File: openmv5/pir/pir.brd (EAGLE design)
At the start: 35.6 x 44.4 mm, 51 parts, among them IC1 AG9905LP, J1 GMJXHT-MM-S-88, J2 OPENMV5-BOTTOM, T1 PT61018PEL

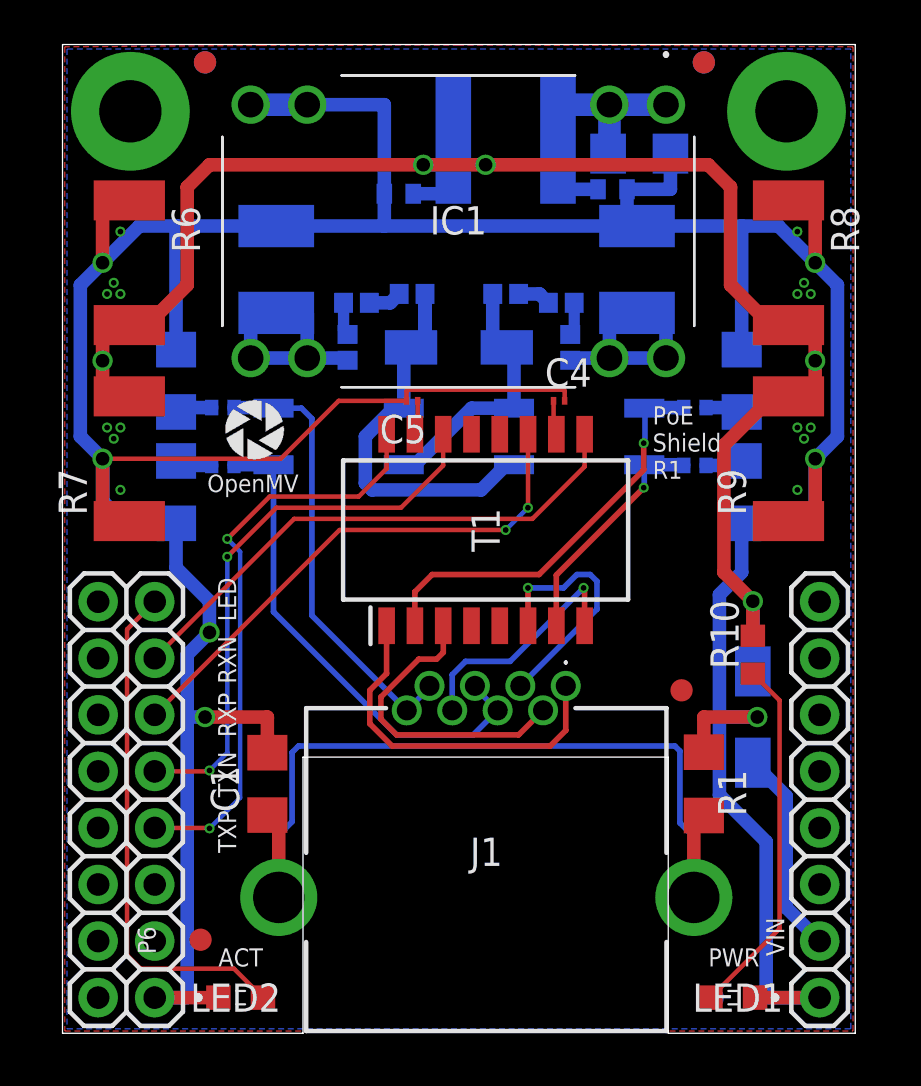
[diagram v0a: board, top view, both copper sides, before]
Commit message: Update PoE Shield heat transfer and add PIR Shield
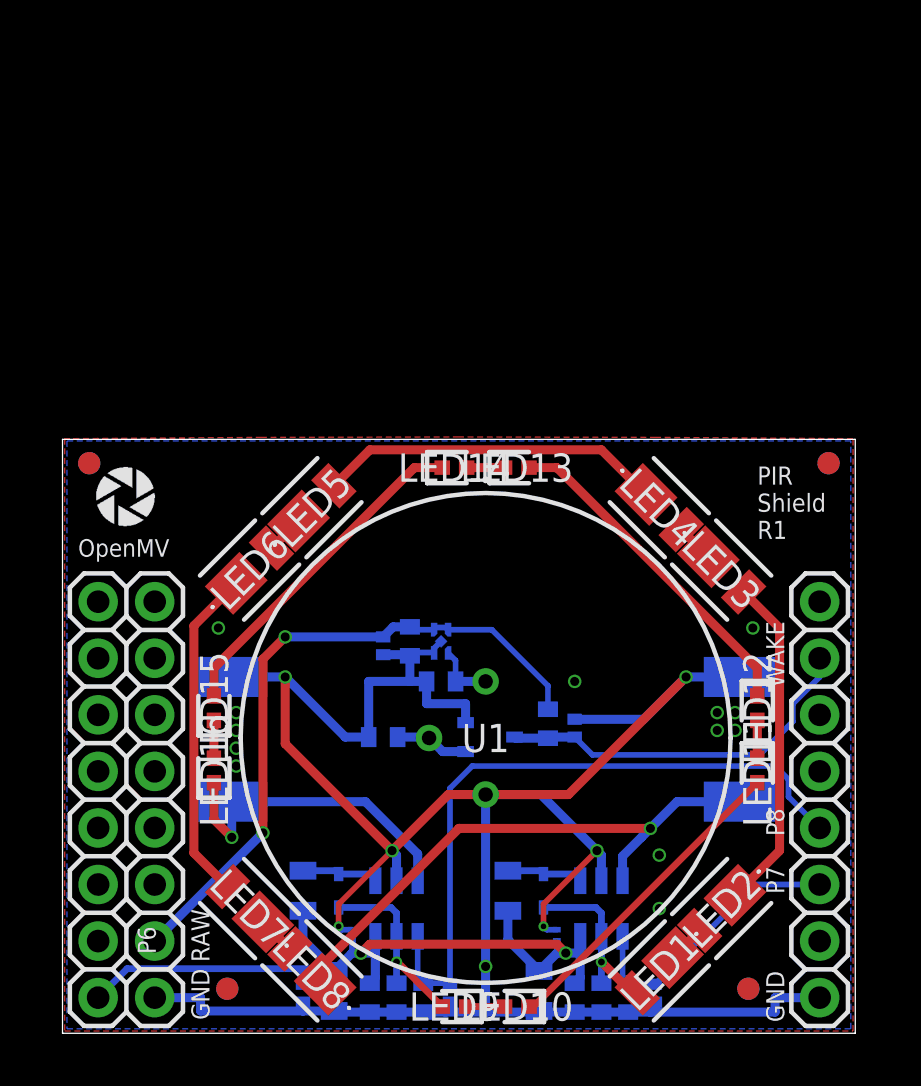
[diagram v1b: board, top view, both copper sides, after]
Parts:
- removed BR1, BR2: MB6S-TP, MB6S-TP:SOP254P665X270-4N
- removed C10, C12, C8, C9: 1nF, rcl:C1206
- removed C11: 10uF, rcl:C0402
- removed J1: GMJXHT-MM-S-88, GMJXHT-MM-S-88:GMJXHTMMS88
- removed L3, L4, L5, L6: 1k, SparkFun-Coils:0402
- removed L7: NR6045T1R8N, NR6045T1R8N:NR6045T1R8N
- removed R10: 470, rcl:R0603
- removed R5: 75, rcl:R0402
- removed R6, R7, R8, R9: 100, rcl:R2512
- removed T1: PT61018PEL, PT61018PEL:SOIC127P930X565-16N
- added C46: 4.7uF, sfe:0402-CAP
- added C48: 0.22uF, rcl:C0201
- added C49: 22uF, SparkFun-Capacitors:0805
- added D3, D4, D6, D9: CPDQT5V0HE-HF, CPDQT5V0HE-HF:CPDQT5V0HEHF
- added D5: RB520S30T5G, RB520S30T5G:SODFL1608X70N
- added IC2: AP3032KTR-G1, AP3032KTR-G1:SOT95P280X145-6N
- added LED10, LED11, LED12, LED13, LED14, LED15, LED16, LED9: SFH_4053, SFH_4053:LEDC1005X55N
- added LED3, LED4, LED5, LED6, LED7, LED8: JB2835AWT-W-U57EA0000-N0000001, JB2835AWT-W-U57EA0000-N0000001:JB2835AWTWU57EA0000N0000001
- added Q4: 2N7002KW_R1_00001, 2N7002KW_R1_00001:SOT65P210X110-3N
- added R24: 100K, sfe:0402-RES
- added R26: 1K, sfe:0402-RES
- added U1: EKMB1307113K, EKMB1304111K:EKMB1304111K
- added U2: MIC5365-3.3YMT-TZ, MIC5365-3.3YMT-TZ:VREG_MIC5365-3.3YMT-TZ
- C1: value 1nF -> 4.7uF; device rcl:C1206 -> sfe:0402-CAP
- C2: value 4.7nF -> 4.7uF; device rcl:C1812 -> sfe:0402-CAP
- C3: value 4.7nF -> 1uF; device rcl:C1812 -> sfe:0402-CAP
- C4: value 0.1uF -> 22uF; device rcl:C0201 -> SparkFun-Capacitors:0805
- C5: value 0.1uF -> 0.22uF
- C6: value 100uF -> 4.7uF; device rcl:C1206 -> sfe:0402-CAP
- C7: value 10uF -> 1uF; device rcl:C0402 -> sfe:0402-CAP
- D1: value SMAJ58A-13-F -> CPDQT5V0HE-HF; device SMAJ58A-13-F:DIOM5226X230N -> CPDQT5V0HE-HF:CPDQT5V0HEHF
- D2: value FM240A -> RB520S30T5G; device FM240A:DIOM5025X231N -> RB520S30T5G:SODFL1608X70N
- IC1: value AG9905LP -> AP3032KTR-G1; device Ag9905LP:AG9905LP -> AP3032KTR-G1:SOT95P280X145-6N
- J2: value OPENMV5-BOTTOM -> OPENMV5-TOP; device openmv5:OPENMV5-BOTTOM -> openmv5:OPENMV5-TOP
- L1, L2: value 1k -> 6.8uH; device SparkFun-Coils:0402 -> SparkFun-Coils:0805
- LED1: value LTST-S270KSKT -> JB2835AWT-W-U57EA0000-N0000001; device LTST-S270K:LTSTS270K -> JB2835AWT-W-U57EA0000-N0000001:JB2835AWTWU57EA0000N0000001
- LED2: value LTST-S270KGKT -> JB2835AWT-W-U57EA0000-N0000001; device LTST-S270K:LTSTS270K -> JB2835AWT-W-U57EA0000-N0000001:JB2835AWTWU57EA0000N0000001
- R1: value 1M -> 100K; device rcl:R1206 -> sfe:0402-RES
- R2, R4: value 75 -> 3.9; device rcl:R0402 -> rcl:R2512
- R3: value 75 -> 100K; device rcl:R0402 -> sfe:0402-RES
- moved C6 39.8 mm to (13.8, 1.60), turned to 90 degrees
- moved C7 37.6 mm to (15.0, 1.60), turned to 90 degrees
- moved IC1 36.2 mm to (24.2, 5.60), flipped to the bottom, turned to 270 degrees
- moved C3 35.8 mm to (24.2, 1.60)
- moved C4 28.4 mm to (12.2, 1.90), flipped to the bottom, turned to 90 degrees
- moved L2 27.2 mm to (10.8, 6.40), turned to 90 degrees
- moved R3 26.8 mm to (16.2, 1.60), turned to 270 degrees
- moved L1 26.8 mm to (20.0, 6.40), turned to 90 degrees
- moved C5 24.2 mm to (13.0, 4.40), flipped to the bottom, turned to 90 degrees
- moved LED2 22.0 mm to (29.6, 5.60), turned to 45 degrees
- moved C2 20.5 mm to (17.0, 15.8), turned to 180 degrees
- moved FD5 18.9 mm to (34.4, 25.6)
- moved FD6 18.9 mm to (34.4, 25.6)
- moved FD7 18.7 mm to (1.20, 25.6)
- moved FD8 18.7 mm to (1.20, 25.6)
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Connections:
- removed net MDI_LED: J2.17, LED2.2
- removed net MDI_RX_CT: C4.1, T1.10
- removed net MDI_RX_N: J2.18, T1.9
- removed net MDI_RX_P: J2.19, T1.11
- removed net MDI_TX_CT: C5.1, T1.15
- removed net MDI_TX_N: J2.20, T1.14
- removed net MDI_TX_P: J2.21, T1.16
- removed net NC1: T1.4
- removed net NC2: T1.5
- removed net NC3: T1.12
- removed net NC4: T1.13
- removed net POE_VIN_INT_N: C2.1, IC1.7, IC1.8, L5.2
- removed net POE_VIN_INT_P: C3.1, IC1.5, IC1.6, L6.2
- removed net POE_VIN_N: BR1.4, BR2.4, D1.2, L1.1
- removed net POE_VIN_N0: L1.2, L3.1
- removed net POE_VIN_N1: L3.2, L5.1
- removed net POE_VIN_P: BR1.3, BR2.3, D1.1, L2.1
- removed net POE_VIN_P0: L2.2, L4.1
- removed net POE_VIN_P1: L4.2, L6.1
- removed net RX_N: J1.6, T1.8
- removed net RX_P: J1.3, T1.6
- removed net SHIELD_GND: C1.1, J1.MH1, J1.MH2, R1.2
- removed net TX_N: J1.2, T1.3
- removed net TX_P: J1.1, T1.1
- removed net VA1: BR1.1, R2.2, T1.2
- removed net VA1_ISO: C8.1, R2.1
- removed net VA2: BR1.2, R3.2, T1.7
- removed net VA2_ISO: C9.1, R3.1
- removed net VB1: BR2.1, J1.4, J1.5, R4.2
- removed net VB1_ISO: C10.1, R4.1
- removed net VB2: BR2.2, J1.7, J1.8, R5.2
- removed net VB2_ISO: C12.1, R5.1
- removed net VDC: C6.1, C7.1, IC1.1, IC1.2, L7.1
- removed net VIN: C11.1, D2.2, L7.2, R10.2, R6.2, R7.2, R8.2, R9.2
- removed net VIN_INT: D2.1, J2.10
- removed net VIN_LED: LED1.2, R10.1
- new net I1: LED10.2, LED9.1
- new net I2: LED10.1, LED11.2
- new net I3: LED11.1, LED12.2
- new net I4: LED12.1, LED13.2
- new net I5: LED13.1, LED14.2
- new net I6: LED14.1, LED15.2
- new net I7: LED15.1, LED16.2
- new net IFB: IC2.3, LED16.1, R4.2
- new net IOV: C7.2, D5.1, IC2.5, LED9.2
- new net ISW: D5.2, IC2.1, L2.2
- new net OUT: Q4.1, R24.1, U1.2
- new net P11_WAKEUP: D9.1, J2.15, Q4.3, R26.1
- new net P7_PWM: D3.1, IC1.4, J2.11, R1.1
- new net P8_PWM: D6.1, IC2.4, J2.12, R3.1
- new net RAW: C1.2, D1.1, J2.23, R26.2, U2.3, U2.4
- new net VCC: C4.2, C46.2, C48.1, C49.2, C5.1, C6.2, D4.1, IC1.6, IC2.6, J2.8, L1.1, L2.1
- new net VDD: C2.2, U1.1, U2.1
- new net W1: LED1.1, LED2.2
- new net W2: LED2.1, LED3.2
- new net W3: LED3.1, LED4.2
- new net W4: LED4.1, LED5.2
- new net W5: LED5.1, LED6.2
- new net W6: LED6.1, LED7.2
- new net W7: LED7.1, LED8.2
- new net WFB: IC1.3, LED8.1, R2.2
- new net WOV: C3.2, D2.1, IC1.5, LED1.2
- new net WSW: D2.2, IC1.1, L1.2
- net GND: now also C1.1, C2.1, C3.1, C4.1, C46.1, C48.2, C49.1, C6.1, C7.1, D1.2, D3.2, D4.2, D6.2, D9.2, IC1.2, IC2.2, Q4.2, R1.2, R2.1, R24.2, R3.2, R4.1, U1.3, U2.2, U2.EP; no longer C1.2, C10.2, C11.2, C12.2, C2.2, C3.2, C4.2, C6.2, C7.2, C8.2, C9.2, IC1.3, IC1.4, LED1.1, LED2.1, R1.1, R6.1, R7.1, R8.1, R9.1
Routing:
- net GND: track 196.3 -> 116.2 mm, vias 23 -> 20
- net VIN: track 74.6 -> 0.00 mm, vias 5 -> 0
- net VCC: track 0.00 -> 39.2 mm, vias 0 -> 2
- net SHIELD_GND: track 39.0 -> 0.00 mm
- net P8_PWM: track 0.00 -> 30.8 mm
- net RAW: track 0.00 -> 30.4 mm, vias 0 -> 2
- net MDI_TX_P: track 26.3 -> 0.00 mm, vias 2 -> 0
- net WFB: track 0.00 -> 25.4 mm, vias 0 -> 1
- net MDI_TX_N: track 25.2 -> 0.00 mm, vias 2 -> 0
- net MDI_RX_N: track 24.3 -> 0.00 mm
- net MDI_RX_P: track 23.9 -> 0.00 mm, vias 2 -> 0
- net MDI_LED: track 23.3 -> 0.00 mm
- net VB1: track 22.7 -> 0.00 mm
- net POE_VIN_P: track 20.3 -> 0.00 mm
- net VB2: track 20.1 -> 0.00 mm
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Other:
- board size 35.6 x 44.4 mm -> 35.6 x 26.7 mm
- board text added: "3.31.23"
- board text added: "P7"
- board text added: "P8"
- board text added: "PIR Shield R1"
- board text added: "RAW"
- board text added: "WAKE"
- board text removed: "3.26.23"
- board text removed: "ACT"
- board text removed: "LED"
- board text removed: "PWR"
- board text removed: "PoE Shield R1"
- board text removed: "RXN"
- board text removed: "RXP"
- board text removed: "TXN"
- board text removed: "TXP"
- board text removed: "VIN"

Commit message: Renumber parts
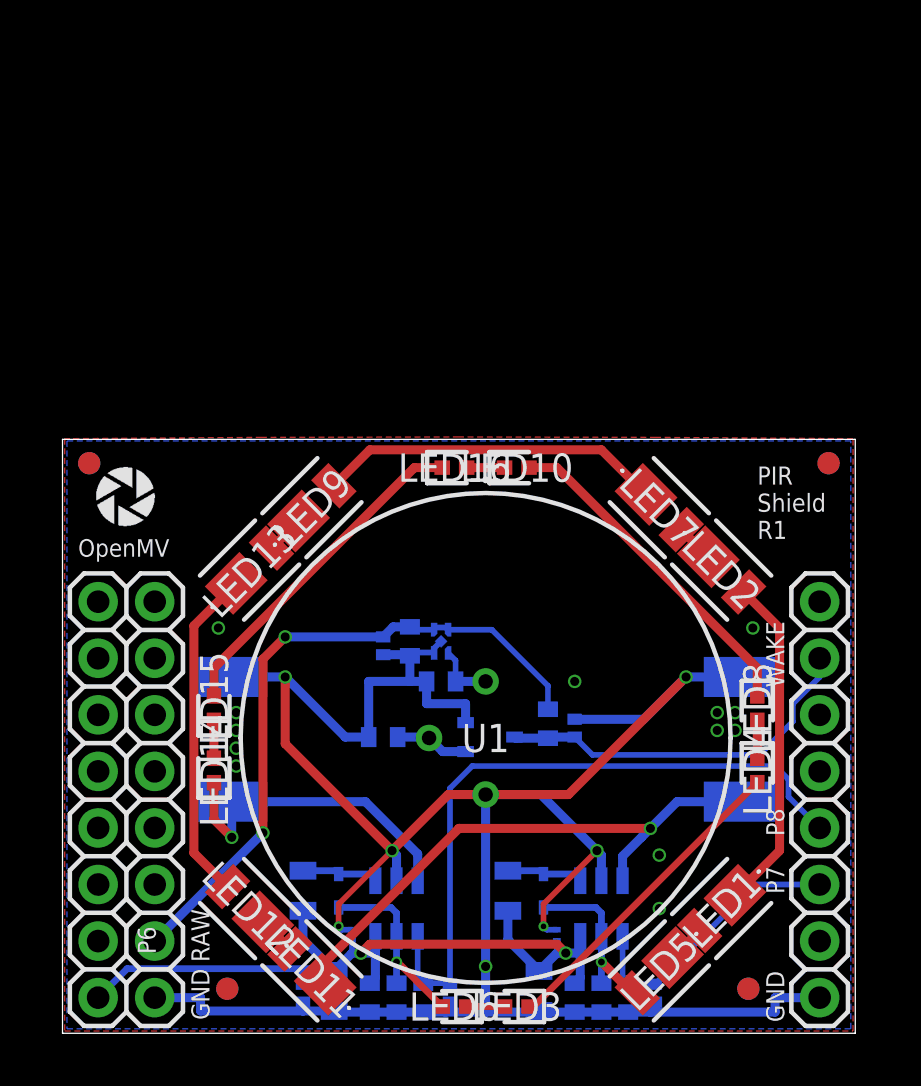
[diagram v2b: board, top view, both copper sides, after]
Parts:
- removed C46: 4.7uF, sfe:0402-CAP
- removed C48: 0.22uF, rcl:C0201
- removed C49: 22uF, SparkFun-Capacitors:0805
- removed D9: CPDQT5V0HE-HF, CPDQT5V0HE-HF:CPDQT5V0HEHF
- added C10, C9: 4.7uF, sfe:0402-CAP
- added C8: 1uF, sfe:0402-CAP
- added D7: CPDQT5V0HE-HF, CPDQT5V0HE-HF:CPDQT5V0HEHF
- C1: value 4.7uF -> 22uF; device sfe:0402-CAP -> SparkFun-Capacitors:0805
- C3, C7: value 1uF -> 0.22uF; device sfe:0402-CAP -> rcl:C0201
- C4: value 22uF -> 1uF; device SparkFun-Capacitors:0805 -> sfe:0402-CAP
- C5: value 0.22uF -> 22uF; device rcl:C0201 -> SparkFun-Capacitors:0805
- D1: value CPDQT5V0HE-HF -> RB520S30T5G; device CPDQT5V0HE-HF:CPDQT5V0HEHF -> RB520S30T5G:SODFL1608X70N
- D5: value RB520S30T5G -> CPDQT5V0HE-HF; device RB520S30T5G:SODFL1608X70N -> CPDQT5V0HE-HF:CPDQT5V0HEHF
- LED11, LED12, LED13, LED9: value SFH_4053 -> JB2835AWT-W-U57EA0000-N0000001; device SFH_4053:LEDC1005X55N -> JB2835AWT-W-U57EA0000-N0000001:JB2835AWTWU57EA0000N0000001
- LED3, LED4, LED6, LED8: value JB2835AWT-W-U57EA0000-N0000001 -> SFH_4053; device JB2835AWT-W-U57EA0000-N0000001:JB2835AWTWU57EA0000N0000001 -> SFH_4053:LEDC1005X55N
- moved FD4 37.9 mm to (1.20, 25.6), flipped to the top
- moved FD5 35.9 mm to (7.40, 2.00), flipped to the bottom
- moved FD7 33.2 mm to (34.4, 25.6), flipped to the bottom
- moved LED5 26.0 mm to (26.8, 2.80), turned to 45 degrees
- moved LED7 25.7 mm to (26.8, 23.6), turned to 135 degrees
- moved LED12 24.5 mm to (8.40, 5.60), turned to 315 degrees
- moved LED10 24.2 mm to (20.4, 25.4), turned to 0 degrees
- moved FD3 23.9 mm to (34.4, 25.6)
- moved FD6 23.9 mm to (30.8, 2.00)
- moved FD2 23.4 mm to (30.8, 2.00), flipped to the top
- moved LED9 23.3 mm to (11.2, 23.6), turned to 225 degrees
- moved LED8 23.2 mm to (31.2, 14.6), turned to 270 degrees
- moved LED11 21.9 mm to (11.2, 2.80), turned to 315 degrees
- moved LED3 21.7 mm to (20.4, 1.20), turned to 180 degrees
- moved LED6 21.7 mm to (17.6, 1.20), turned to 180 degrees
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- renumbered J2 to J1, Q4 to Q1, R24 to R6, R26 to R5
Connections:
- net GND: now also C10.1, C3.2, C5.1, C7.2, C8.1, C9.1, D5.2, D7.2; no longer C3.1, C46.1, C48.2, C49.1, C5.2, C7.1, D1.2, D9.2
- net I1: now also LED3.2, LED6.1; no longer LED10.2, LED9.1
- net I2: now also LED3.1, LED4.2; no longer LED10.1, LED11.2
- net I3: now also LED4.1, LED8.2; no longer LED11.1, LED12.2
- net I4: now also LED10.2, LED8.1; no longer LED12.1, LED13.2
- net I5: now also LED10.1, LED16.2; no longer LED13.1, LED14.2
- net I6: now also LED16.1; no longer LED14.1
- net I7: now also LED14.2; no longer LED16.2
- net IFB: now also LED14.1; no longer LED16.1
- net IOV: now also C8.2, D2.1, LED6.2; no longer C7.2, D5.1, LED9.2
- net ISW: now also D2.2; no longer D5.2
- net P11_WAKEUP: now also D6.1; no longer D9.1
- net P8_PWM: now also D4.1; no longer D6.1
- net RAW: now also C9.2, D7.1; no longer C1.2, D1.1
- net VCC: now also C1.2, C2.2, C3.1, C5.2, C7.1, D5.1; no longer C4.2, C46.2, C48.1, C49.2, C5.1, D4.1
- net VDD: now also C10.2; no longer C2.2
- net W1: now also LED1.2, LED5.1; no longer LED1.1, LED2.2
- net W2: now also LED1.1, LED2.2; no longer LED2.1, LED3.2
- net W3: now also LED2.1, LED7.2; no longer LED3.1, LED4.2
- net W4: now also LED7.1, LED9.2; no longer LED4.1, LED5.2
- net W5: now also LED13.2, LED9.1; no longer LED5.1, LED6.2
- net W6: now also LED12.2, LED13.1; no longer LED6.1, LED7.2
- net W7: now also LED11.2, LED12.1; no longer LED7.1, LED8.2
- net WFB: now also LED11.1; no longer LED8.1
- net WOV: now also C4.2, D1.1, LED5.2; no longer C3.2, D2.1, LED1.2
- net WSW: now also D1.2; no longer D2.2
